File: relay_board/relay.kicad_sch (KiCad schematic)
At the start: 35 parts, among them J2 ACT_PWR, J3 ACT_PWR, J4 Actuator, U3 T9GV1L14-12, U4 T92S11D12-12, U5 LTV-356T, U6 LTV-356T, U7 INA180, U8 INA180

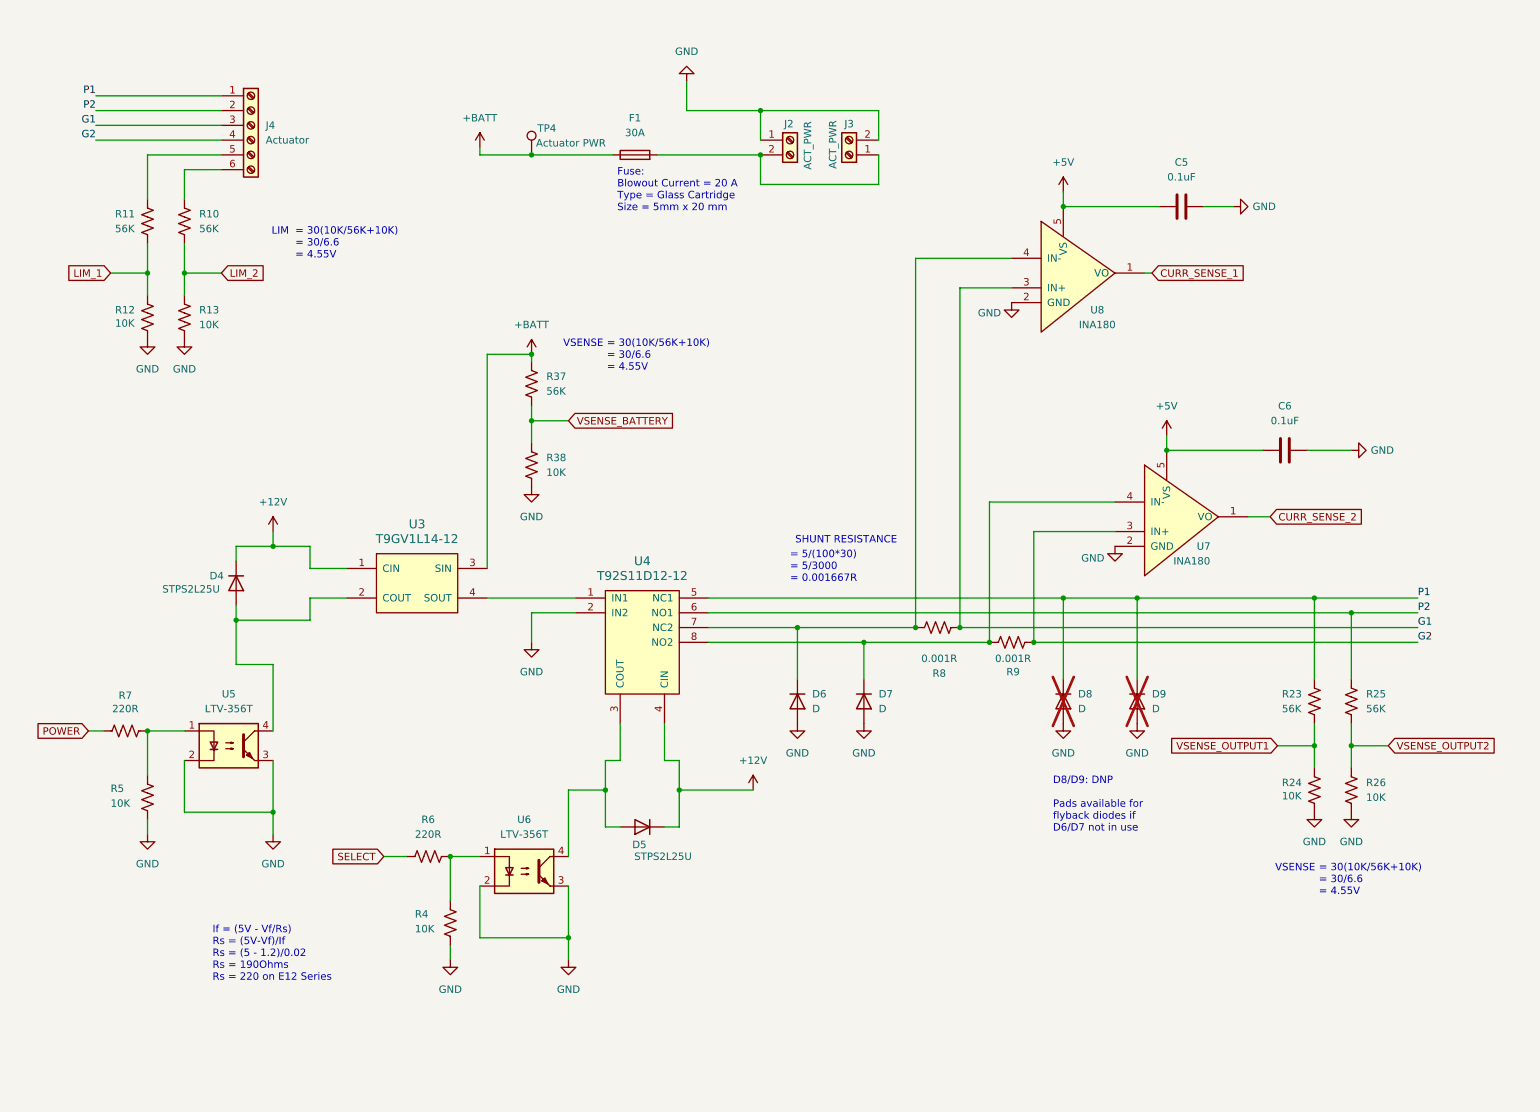
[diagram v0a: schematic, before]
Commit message: Changed to Hierarchical labels and added reverse voltage protection. Still need to do resistor math for voltage protection.
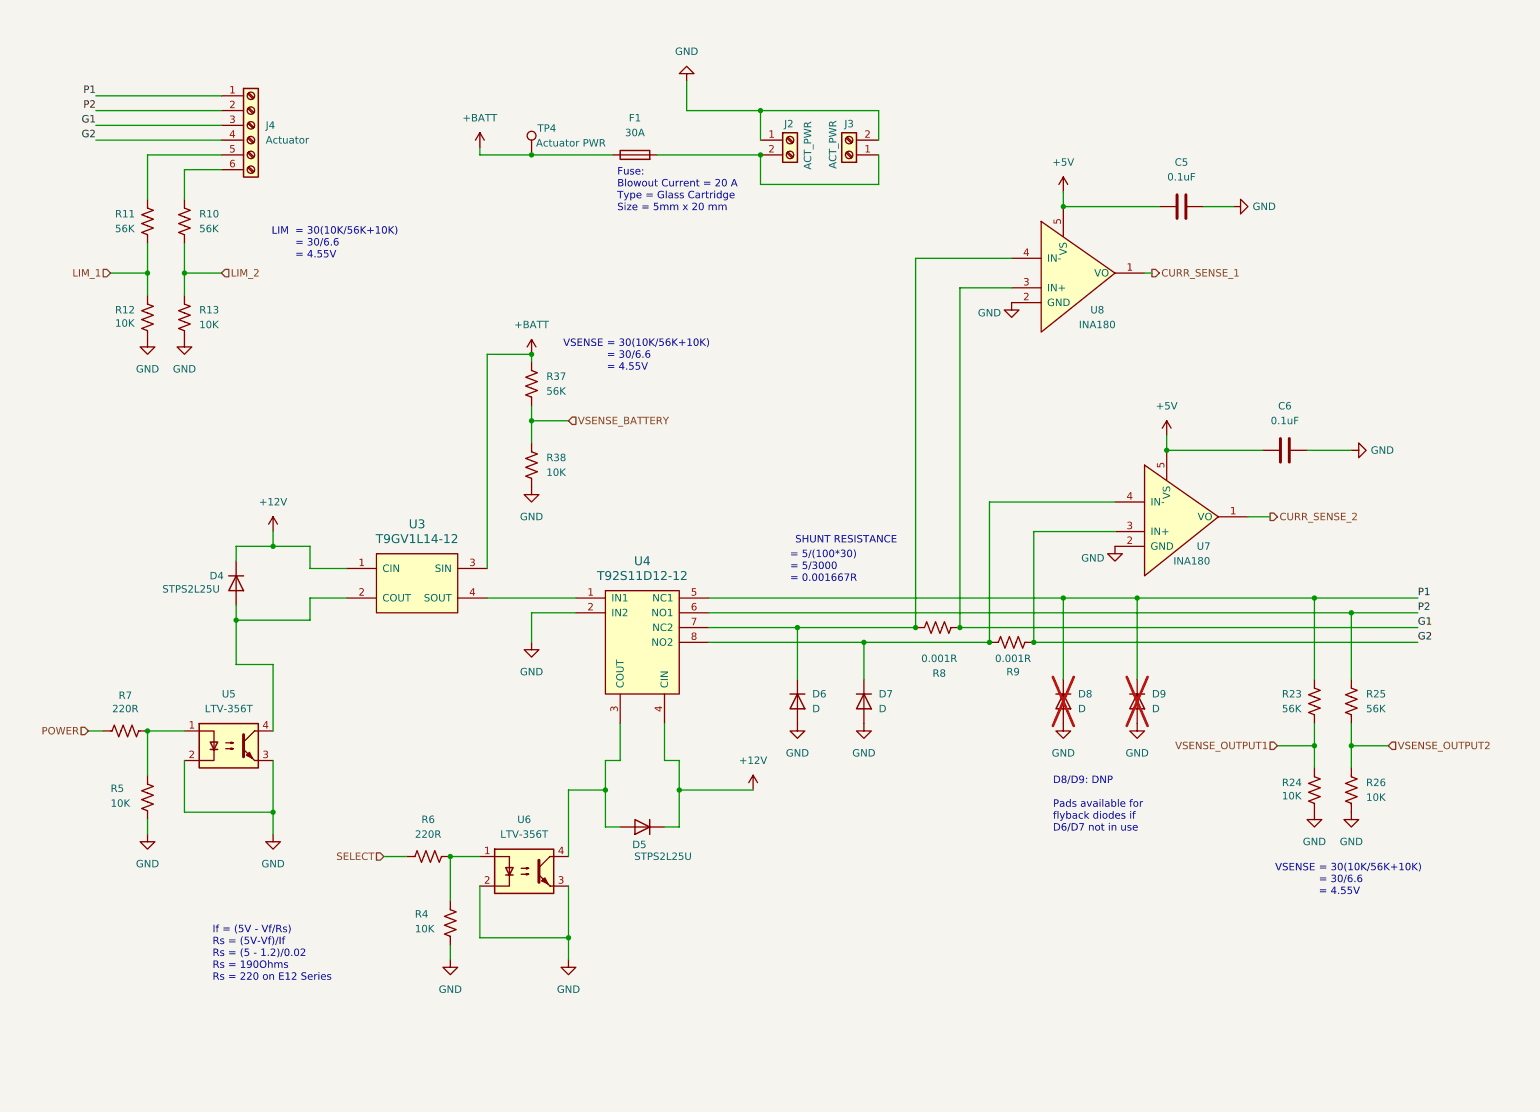
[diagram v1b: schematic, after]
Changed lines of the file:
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@@
 		)
 	)
-	(global_label "CURR_SENSE_2"
+	(hierarchical_label "POWER"
 		(shape input)
-		(at 228.6 99.06 0)
-		(fields_autoplaced yes)
+		(at 25.4 135.89 180)
+		(effects
+			(font
+				(size 1.27 1.27)
+			)
+			(justify right)
+		)
+	)
+	(hierarchical_label "LIM_2"
+		(shape input)
+		(at 48.26 57.15 0)
 		(effects
 			(font
@@
 			(justify left)
 		)
-		(property "Intersheetrefs" "${INTERSHEET_REFS}"
-			(at 245.9179 99.06 0)
-			(effects
-				(font
-					(size 1.27 1.27)
-				)
-				(justify left)
-				(hide yes)
-			)
-		)
 	)
-	(global_label "VSENSE_OUTPUT2"
+	(hierarchical_label "VSENSE_OUTPUT2"
 		(shape input)
 		(at 248.92 138.43 0)
-		(fields_autoplaced yes)
 		(effects
 			(font
@@
 			(justify left)
 		)
-		(property "Intersheetrefs" "${INTERSHEET_REFS}"
-			(at 268.4151 138.43 0)
-			(effects
-				(font
-					(size 1.27 1.27)
-				)
-				(justify left)
-				(hide yes)
+	)
+	(hierarchical_label "CURR_SENSE_2"
+		(shape output)
+		(at 228.6 99.06 0)
+		(effects
+			(font
+				(size 1.27 1.27)
 			)
+			(justify left)
 		)
 	)
-	(global_label "VSENSE_OUTPUT1"
+	(hierarchical_label "SELECT"
 		(shape input)
-		(at 229.87 138.43 180)
-		(fields_autoplaced yes)
+		(at 76.2 157.48 180)
 		(effects
 			(font
@@
 			(justify right)
 		)
-		(property "Intersheetrefs" "${INTERSHEET_REFS}"
-			(at 210.3749 138.43 0)
-			(effects
-				(font
-					(size 1.27 1.27)
-				)
-				(justify right)
-				(hide yes)
-			)
-		)
 	)
-	(global_label "SELECT"
+	(hierarchical_label "VSENSE_OUTPUT1"
 		(shape input)
-		(at 76.2 157.48 180)
-		(fields_autoplaced yes)
+		(at 229.87 138.43 180)
 		(effects
 			(font
@@
 			(justify right)
 		)
-		(property "Intersheetrefs" "${INTERSHEET_REFS}"
-			(at 66.4416 157.48 0)
-			(effects
-				(font
-					(size 1.27 1.27)
-				)
-				(justify right)
-				(hide yes)
-			)
-		)
 	)
-	(global_label "LIM_1"
+	(hierarchical_label "LIM_1"
 		(shape input)
 		(at 29.21 57.15 180)
-		(fields_autoplaced yes)
 		(effects
 			(font
@@
 			(justify right)
 		)
-		(property "Intersheetrefs" "${INTERSHEET_REFS}"
-			(at 20.9634 57.15 0)
-			(effects
-				(font
-					(size 1.27 1.27)
-				)
-				(justify right)
-				(hide yes)
-			)
-		)
 	)
-	(global_label "LIM_2"
-		(shape input)
-		(at 48.26 57.15 0)
-		(fields_autoplaced yes)
+	(hierarchical_label "CURR_SENSE_1"
+		(shape output)
+		(at 208.28 57.15 0)
 		(effects
 			(font
@@
 			(justify left)
 		)
-		(property "Intersheetrefs" "${INTERSHEET_REFS}"
-			(at 56.5066 57.15 0)
-			(effects
-				(font
-					(size 1.27 1.27)
-				)
-				(justify left)
-				(hide yes)
-			)
-		)
 	)
-	(global_label "CURR_SENSE_1"
+	(hierarchical_label "VSENSE_BATTERY"
 		(shape input)
-		(at 208.28 57.15 0)
-		(fields_autoplaced yes)
+		(at 107.95 82.55 0)
 		(effects
 			(font
@@
 			(justify left)
 		)
-		(property "Intersheetrefs" "${INTERSHEET_REFS}"
-			(at 225.5979 57.15 0)
-			(effects
-				(font
-					(size 1.27 1.27)
-				)
-				(justify left)
-				(hide yes)
-			)
-		)
 	)
-	(global_label "VSENSE_BATTERY"
-		(shape input)
-		(at 107.95 82.55 0)
-		(fields_autoplaced yes)
-		(effects
-			(font
-				(size 1.27 1.27)
-			)
-			(justify left)
-		)
-		(property "Intersheetrefs" "${INTERSHEET_REFS}"
-			(at 126.8403 82.55 0)
-			(effects
-				(font
-					(size 1.27 1.27)
-				)
-				(justify left)
-				(hide yes)
-			)
-		)
-	)
-	(global_label "POWER"
-		(shape input)
-		(at 25.4 135.89 180)
-		(fields_autoplaced yes)
-		(effects
-			(font
-				(size 1.27 1.27)
-			)
-			(justify right)
-		)
-		(property "Intersheetrefs" "${INTERSHEET_REFS}"
-			(at 15.9439 135.89 0)
-			(effects
-				(font
-					(size 1.27 1.27)
-				)
-				(justify right)
-				(hide yes)
-			)
-		)
-	)

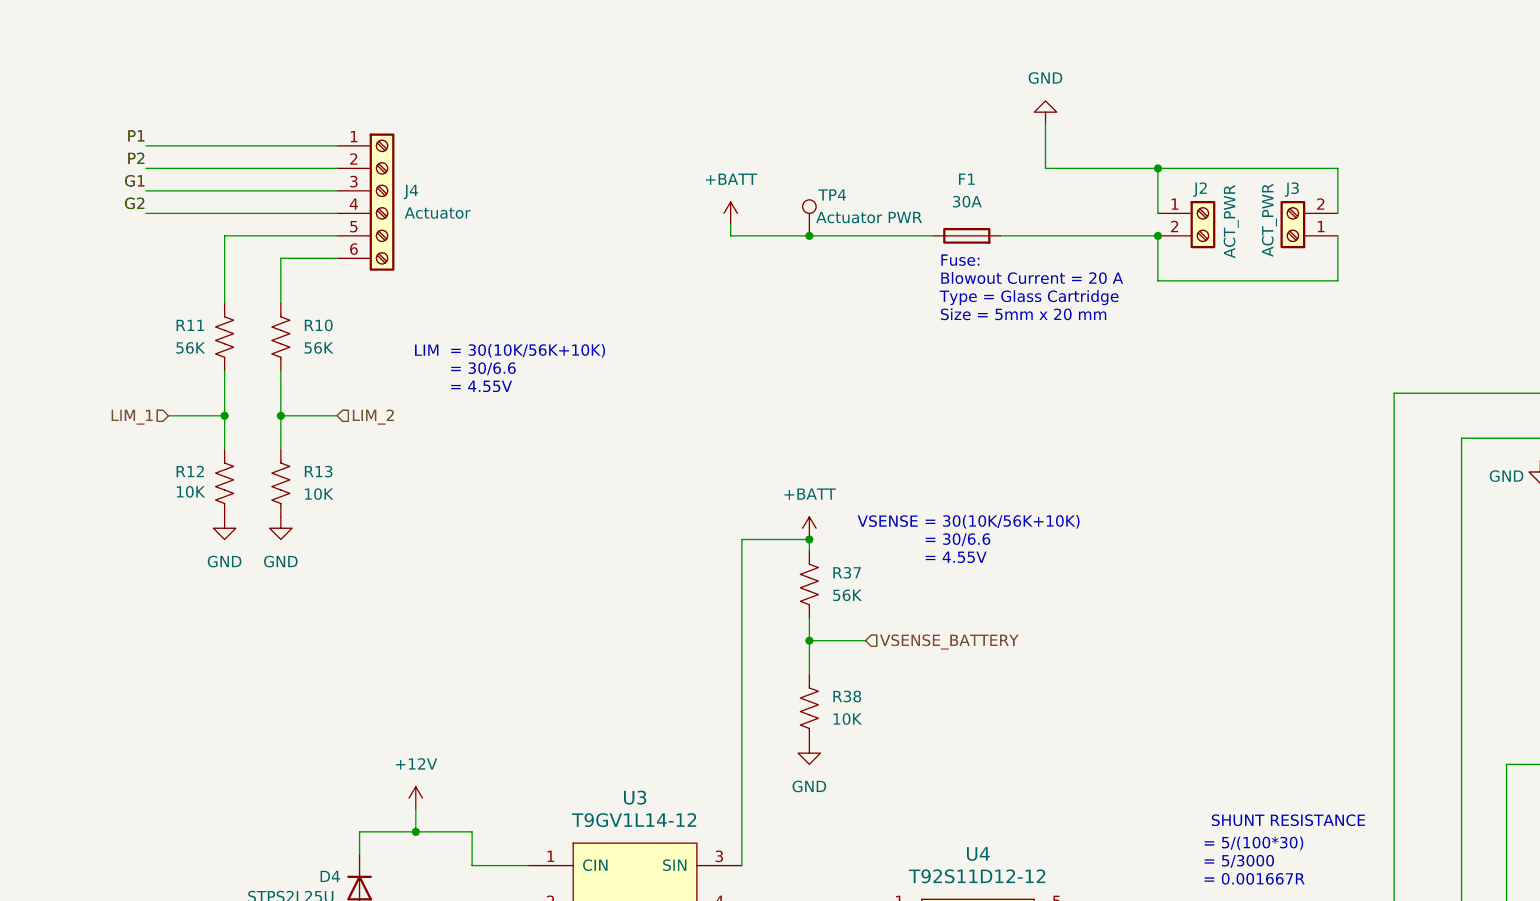
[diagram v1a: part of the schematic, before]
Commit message: Finished Reverse Voltage Math, added labels
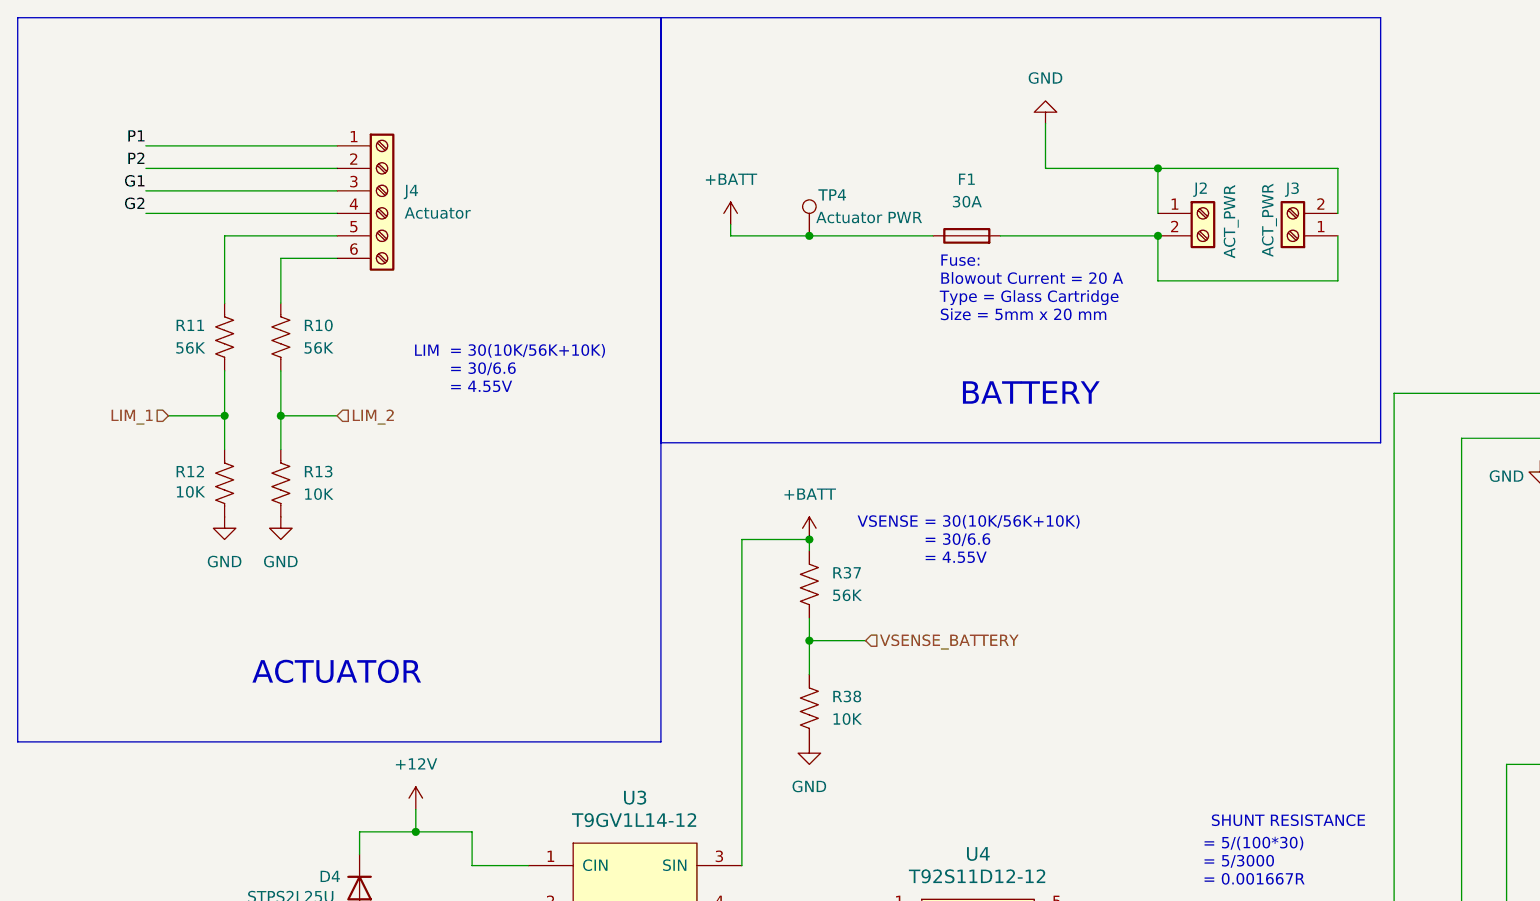
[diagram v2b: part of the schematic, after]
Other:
- note added: "ACTUATOR"
- note added: "BATTERY"
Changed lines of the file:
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@@
+		)
+	)
+	(rectangle
+		(start 12.192 12.192)
+		(end 84.836 93.98)
+		(stroke
+			(width 0)
+			(type default)
+		)
+		(fill
+			(type none)
+		)
+	)
+	(rectangle
+		(start 84.836 12.192)
+		(end 166.116 60.198)
+		(stroke
+			(width 0)
+			(type default)
+		)
+		(fill
+			(type none)
 		)
 	)
@@
 		)
 	)
+	(text "ACTUATOR"
+		(exclude_from_sim no)
+		(at 48.26 86.36 0)
+		(effects
+			(font
+				(size 2.54 2.54)
+				(thickness 0.3175)
+			)
+		)
+	)
 	(text "D8/D9: DNP\n\nPads available for \nflyback diodes if \nD6/D7 not in use"
 		(exclude_from_sim no)
@@
 		)
 	)
+	(text "BATTERY"
+		(exclude_from_sim no)
+		(at 126.492 54.864 0)
+		(effects
+			(font
+				(size 2.54 2.54)
+			)
+		)
+	)

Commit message: requested changes 1
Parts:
- removed U5, U6: LTV-356T, Package_SO:SO-4_4.4x3.6mm_P2.54mm, symbol Isolator:LTV-356T
- added K1, K2: PS2702-1-F3-A, relay_board:SO4_PS2702-1_REN, symbol PS2702-1:PS2702-1-F3-A
- D6, D7, D8, D9: value D -> STPS2L25U
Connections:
- net GND: now also K1.2, K1.3, K2.2, K2.3
- net at D5.2 (A), U4.3 (COUT): now also K2.4
- net at R5.1, R7.2: now also K1.1
- net at R4.1, R6.2: now also K2.1
- net at D4.2 (A), U3.2 (COUT): now also K1.4
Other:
- note added: "12/(77.4) = 155mA"
- moved on the sheet: R4, R5, R6, R7

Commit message: fix symbols; routing v1
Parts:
- removed U3: T9GV1L14-12, footprints:T9GV1L1412, symbol relay_board:SPST_POWER_RELAY
- removed U4: T92S11D12-12, footprints:RELAY8-T92-MODULE, symbol relay_board:dpdt_relay
- added K3: T9GV1L14-12, relay_board:T9GV1L1412, symbol T9GV1L14-12:T9GV1L14-12
- F1: footprint footprints:3557-10_KEY -> relay_board:3557-10_KEY
- R8, R9: footprint Resistor_SMD:R_0805_2012Metric_Pad1.20x1.40mm_HandSolder -> Resistor_SMD:R_2512_6332Metric_Pad1.40x3.35mm_HandSolder
- U7, U8: value INA180 -> INA180A3
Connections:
- net +12V: now also K3.1 (COIL_1)
- net +BATT: now also K3.5 (NO)
- net P1: no longer D9.1 (K)
- net P2: now also D9.1 (K)
- net T92S11D12-12/COUT: now reaches D5.2 (A), K2.4
- net T92S11D12-12/NC2: now reaches D6.1 (K), R8.1, U8.4 (IN-)
- net T92S11D12-12/NO2: now reaches D7.1 (K), R9.1, U7.4 (IN-)
- net at D4.2 (A), K1.4: now also K3.2 (COIL_2)
- new net T92S11D12-12/COM1: K3.3 (COM)
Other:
- added sheet T92S11D12-12 (t92s.kicad_sch)
- moved on the sheet: D5, D6, D7, K2, R37, R38, R4, R6
